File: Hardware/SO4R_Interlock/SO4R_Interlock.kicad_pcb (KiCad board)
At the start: 4 copper layers, 67.4 x 100.7 mm, 143 parts, among them J1 USB-C 2.0 16P, J2 USB-C 2.0 16P, J3 USB-C 2.0 16P, J4 USB-C 2.0 16P, J5 Header 1x3, J6 RJ45_LED_Shielded, J7 8P8C_LED_Shielded_x4, Q1 2N7002, Q2 2N7002, Q3 2N7002, Q4 2N7002, Q5 2N7002, Q6 2N7002, Q7 2N7002, Q8 2N7002, U1 FT230XS, U10 TPD4E02B04DQA, U11 TPD4E02B04DQA, U12 TPD4E02B04DQA, U2 FT230XS, U3 FT230XS, U4 FT230XS, U5 74LVC1G07, U6 74LVC1G07, U7 74LVC1G07, U8 AVR32DB48x-xPT, U9 TPD4E02B04DQA

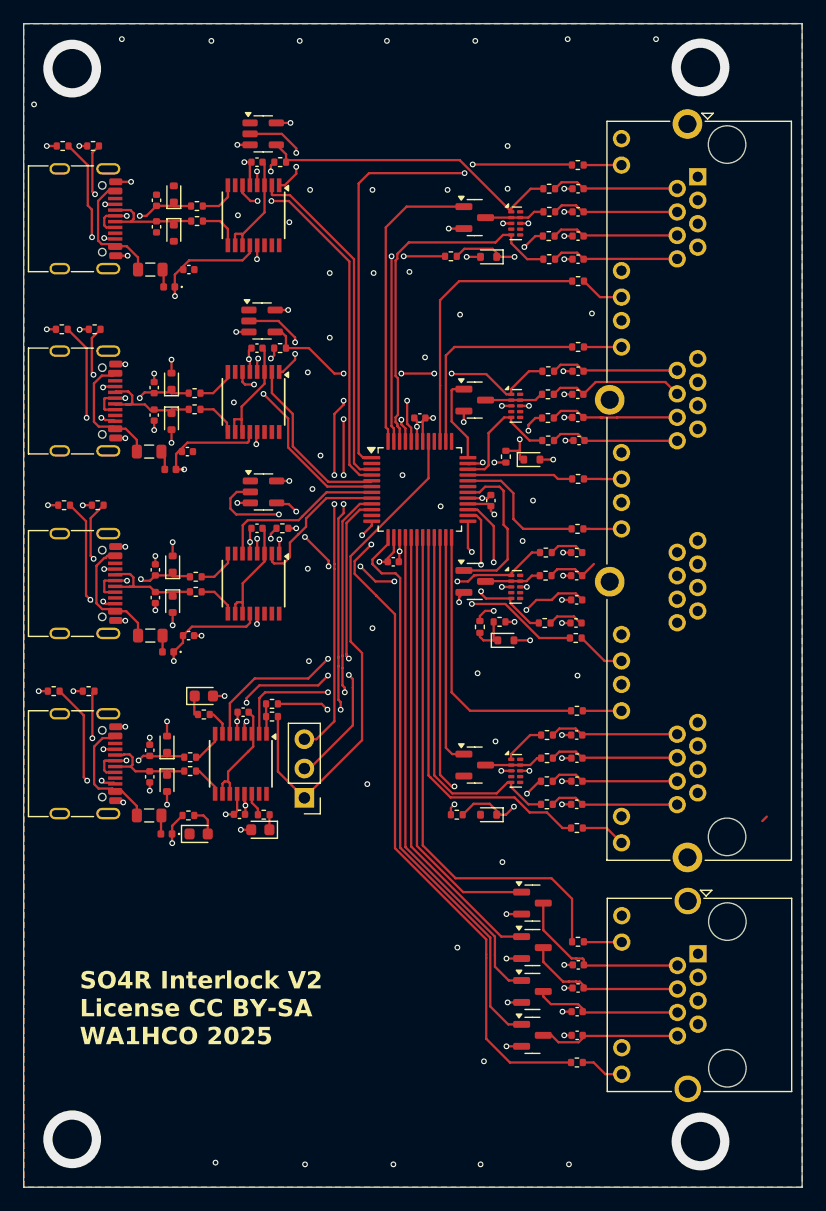
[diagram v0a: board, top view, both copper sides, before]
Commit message: V2 Files sent to JLCPCB Relays are driven by 12V Relay driver has diagnostic interface to MCU Diode combine 12V from rig interface or barrel jack
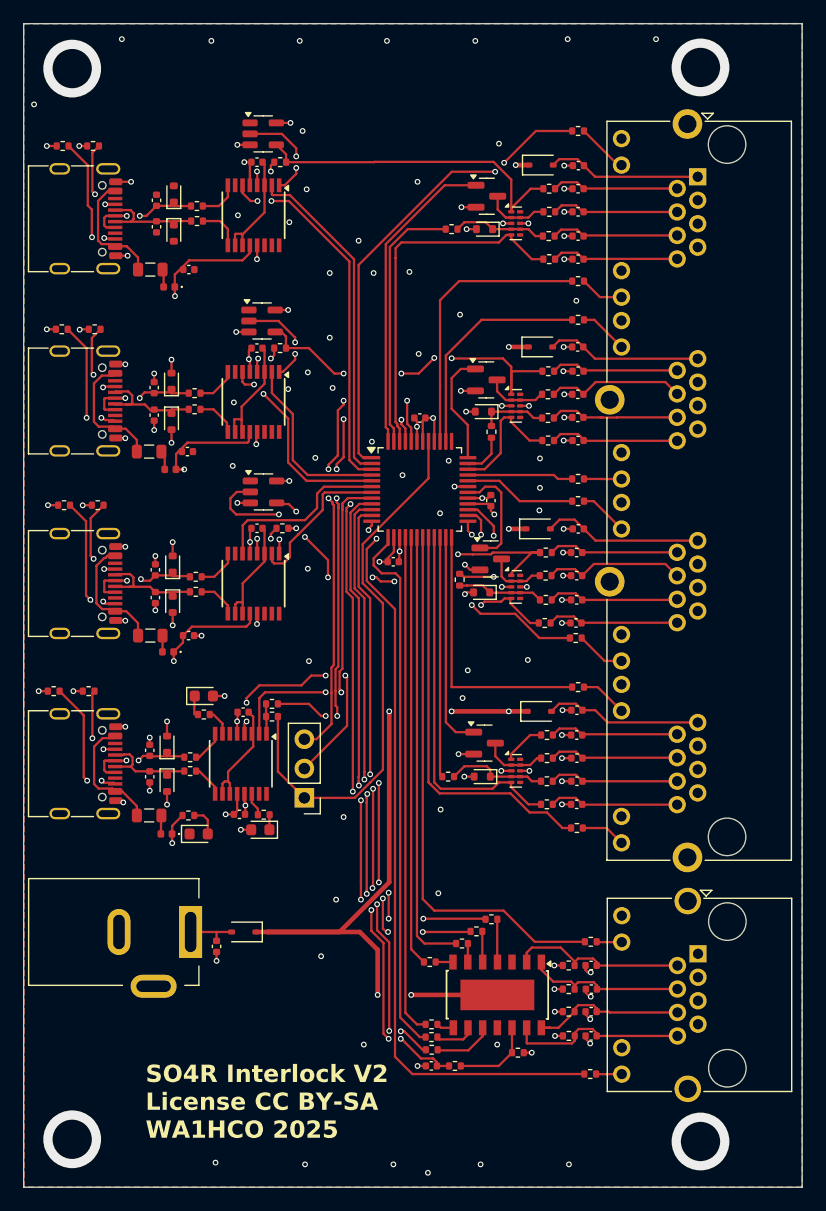
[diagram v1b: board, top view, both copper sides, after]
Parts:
- removed the C19 at (151.2, 131.5)
- removed the C21 at (151.1, 133.6)
- removed the C22 at (151.1, 135.6)
- removed the Q1 at (147.2, 124.2)
- removed the Q2 at (147.2, 128.0)
- removed the Q3 at (147.2, 131.8)
- removed the Q4 at (147.2, 135.6)
- added C1: .1u, Capacitor_SMD:C_0402_1005Metric, F.Cu at (119.9, 127.9)
- added C30: .1u, Capacitor_SMD:C_0402_1005Metric, F.Cu at (151.2, 60.3)
- added C32: .1u, Capacitor_SMD:C_0402_1005Metric, F.Cu at (151.2, 76.0)
- added C34: .1u, Capacitor_SMD:C_0402_1005Metric, F.Cu at (151.2, 91.8)
- added C36: .1u, Capacitor_SMD:C_0402_1005Metric, F.Cu at (151.1, 107.5)
- added C42: .1u, Capacitor_SMD:C_0402_1005Metric, F.Cu at (152.3, 135.7)
- added C43: .1u, Capacitor_SMD:C_0402_1005Metric, F.Cu at (152.3, 133.6)
- added C44: .1u, Capacitor_SMD:C_0402_1005Metric, F.Cu at (152.3, 129.6)
- added C45: .1u, Capacitor_SMD:C_0402_1005Metric, F.Cu at (152.3, 131.6)
- added D21: BAS316, Diode_SMD:D_SOD-323, F.Cu at (148.0, 60.2)
- added D22: BAS316, Diode_SMD:D_SOD-323, F.Cu at (147.8, 107.5)
- added D23: BAS316, Diode_SMD:D_SOD-323, F.Cu at (147.9, 76.0)
- added D24: BAS316, Diode_SMD:D_SOD-323, F.Cu at (147.8, 91.8)
- added D5: BAS316, Diode_SMD:D_SOD-323, F.Cu at (122.2, 126.7)
- added J1: 12V, Connector_BarrelJack:BarrelJack_Kycon_KLDX-0202-xC_Horizontal, F.Cu at (117.7, 126.7)
- added R25: 4K7, Resistor_SMD:R_0402_1005Metric, F.Cu at (140.5, 138.2)
- added R26: 10K, Resistor_SMD:R_0402_1005Metric, F.Cu at (138.5, 136.8)
- added R27: 10K, Resistor_SMD:R_0402_1005Metric, F.Cu at (138.4, 129.2)
- added R28: 10K, Resistor_SMD:R_0402_1005Metric, F.Cu at (141.2, 127.7)
- added R29: 10K, Resistor_SMD:R_0402_1005Metric, F.Cu at (138.5, 134.7)
- added R30: 10K, Resistor_SMD:R_0402_1005Metric, F.Cu at (138.5, 135.8)
- added R31: 10K, Resistor_SMD:R_0402_1005Metric, F.Cu at (142.4, 126.6)
- added R32: 10K, Resistor_SMD:R_0402_1005Metric, F.Cu at (143.7, 125.5)
- added R33: 1K2, Resistor_SMD:R_0402_1005Metric, F.Cu at (146.0, 137.1)
- added R34: 47k, Resistor_SMD:R_0402_1005Metric, F.Cu at (150.4, 135.7)
- added R35: 47K, Resistor_SMD:R_0402_1005Metric, F.Cu at (150.4, 133.6)
- added R36: 47K, Resistor_SMD:R_0402_1005Metric, F.Cu at (150.4, 129.6)
- added R37: 47K, Resistor_SMD:R_0402_1005Metric, F.Cu at (150.4, 131.6)
- added U8: BTS5200-4EKA, Interlock:Infineon_PG-DSO-14-48-EP, F.Cu at (144.2, 132.1)
- C18: value .1u -> 100p
- moved C18 15.4 mm to (138.5, 138.2), turned to 180 degrees
- moved D18 5.90 mm to (143.0, 81.6), turned to 180 degrees
- moved D19 4.65 mm to (142.8, 97.2), turned to 180 degrees
- moved R42 4.45 mm to (140.9, 96.2)
- moved R54 4.44 mm to (148.4, 97.9)
- moved R43 3.38 mm to (139.9, 113.2)
- moved D20 3.35 mm to (142.9, 113.2)
- moved R61 2.95 mm to (151.2, 57.3)
- moved R41 2.49 mm to (143.7, 83.3)
- moved D17 2.43 mm to (143.1, 65.8)
- moved R65 2.40 mm to (151.2, 89.3)
- moved Q3 2.39 mm to (143.6, 94.3)
- moved R40 2.35 mm to (140.2, 65.8)
- moved R63 2.35 mm to (151.2, 73.7)
- moved Q1 2.13 mm to (143.3, 63.0)
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- renumbered C9 to C10, C10 to C11, C11 to C12, C12 to C13, C13 to C14, C14 to C15, C15 to C16, C16 to C17, C17 to C19, C1 to C2, C23 to C21, C24 to C22, C25 to C23, C26 to C24, C27 to C25, C28 to C26, C29 to C27, C30 to C28, C31 to C29, C2 to C3, C32 to C31, C34 to C35, C35 to C37, C36 to C38, C37 to C39, C3 to C4, C38 to C40, C39 to C41, C4 to C5, C5 to C6, C6 to C7, C7 to C8, C8 to C9, D9 to D10, D10 to D11, D11 to D12, D12 to D13, D13 to D14, D14 to D15, D15 to D16, D19 to D17, D16 to D19, D17 to D20, D5 to D6, D6 to D7, D7 to D8, D8 to D9, J1 to J2, J2 to J3, J3 to J4, J4 to J5, J5 to J6, J6 to J7, J7 to J8, Q6 to Q1, Q7 to Q2, Q8 to Q3, Q5 to Q4, R26 to R38, R25 to R39, R57 to R40, R55 to R41, R52 to R42, R53 to R43, R27 to R44, R28 to R45, R58 to R46, R30 to R47, R31 to R48, R32 to R49, R56 to R50, R34 to R51, R35 to R52, R36 to R53, R51 to R54, R38 to R55, R39 to R56, R40 to R57, R54 to R58, R42 to R59, R43 to R60, R44 to R61, R45 to R62, R46 to R63, R47 to R64, R48 to R65, R49 to R66, R50 to R67, U9 to U10, U10 to U11, U11 to U12, U12 to U13, U8 to U9
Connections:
- C18 pad 1: GND -> /IS
- C18 pad 2: Net-(Q1-D) -> GND
- J7 pad 2: Net-(Q1-D) -> Net-(U8-OUT1)
- J8 pad 1: GND -> Net-(D21-A)
- J8 pad 13: GND -> Net-(D23-A)
- J8 pad 25: GND -> Net-(D24-A)
- J8 pad 37: GND -> Net-(D22-A)
- U10 pad 4: unconnected-(U9-IO3-Pad4) -> /KEY4\
- U11 pad 4: unconnected-(U10-IO3-Pad4) -> /KEY3\
- U12 pad 4: unconnected-(U11-IO3-Pad4) -> /KEY2\
- U13 pad 4: unconnected-(U12-IO3-Pad4) -> /KEY1\
- U4 pad 6: /CTS1\ -> unconnected-(U4-~{CTS}-Pad6)
- U9 pad 10: /CTS1\ -> /DSEL0
- U9 pad 11: unconnected-(U8-PC1-Pad11) -> /DSEL1
- U9 pad 2: unconnected-(U8-PA6-Pad2) -> /RTS4\
- U9 pad 3: /RTS4\ -> /CTS4\
- U9 pad 31: unconnected-(U8-PE1-Pad31) -> /IS
- U9 pad 4: /CTS4\ -> /RTS3\
- U9 pad 5: /RTS3\ -> /CTS3\
- U9 pad 6: /CTS3\ -> /CTS2\
- U9 pad 7: /CTS2\ -> /RTS2\
- U9 pad 8: /RTS2\ -> /RTS1\
- U9 pad 9: /RTS1\ -> /DEN
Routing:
- net /12V: track 0.00 -> 117.9 mm, vias 0 -> 8
- net /IS: track 0.00 -> 65.2 mm, vias 0 -> 8
- net /DEN: track 0.00 -> 52.5 mm, vias 0 -> 6
- net /DSEL0: track 0.00 -> 46.6 mm, vias 0 -> 6
- net /DSEL1: track 0.00 -> 45.5 mm, vias 0 -> 6
- net /CTS1\: track 29.6 -> 0.00 mm, vias 2 -> 0
- net Net-(U8-OUT1): track 0.00 -> 15.8 mm
- net Net-(Q1-D): track 15.5 -> 0.00 mm
- net Net-(D24-A): track 0.00 -> 13.8 mm
- net Net-(D22-A): track 0.00 -> 13.6 mm
- net Net-(D23-A): track 0.00 -> 13.5 mm
- net Net-(D21-A): track 0.00 -> 13.4 mm
- net Net-(C40-Pad2): track 3.18 -> 11.4 mm
- net Net-(C24-Pad2): track 3.14 -> 11.3 mm
- net Net-(C28-Pad2): track 4.62 -> 12.3 mm
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
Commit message: 2nd try at submitting to JLCPBC, this is hardware V2.1 V2 added BTS5200 relay driver chip, 4 channels Corrected footprints Adjusted HardwareConfig.h to adapt to new pins related to adding relay driver chip Software now has the ability detect faults on relay lines
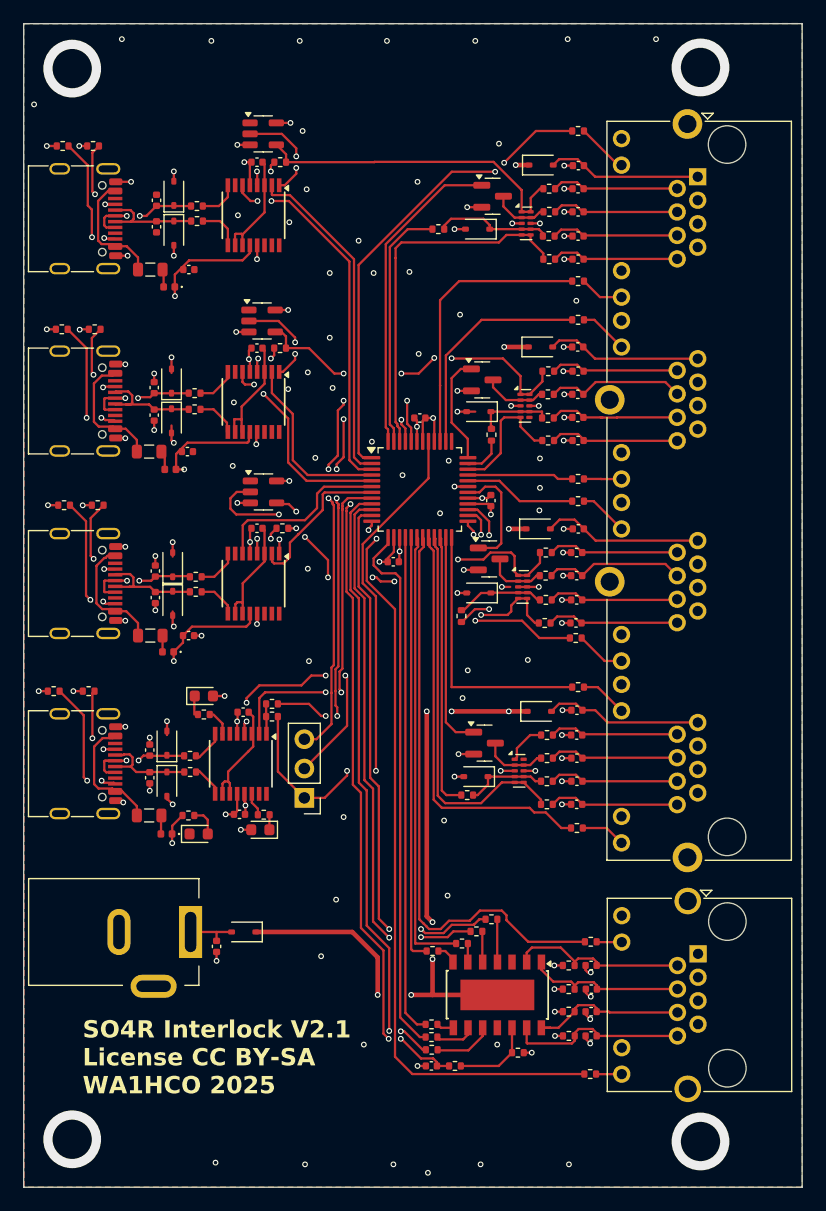
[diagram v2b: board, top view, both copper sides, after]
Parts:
- D1, D10, D11, D12, D13, D17, D18, D19, D2, D20, D3, D4: footprint Diode_SMD:D_SOD-523 -> Diode_SMD:D_SOD-323
- moved R42 3.15 mm to (141.1, 99.3), turned to -90 degrees
- moved R43 2.30 mm to (141.6, 114.8)
- moved R40 1.15 mm to (139.1, 65.8)
- moved R27 0.98 mm to (138.6, 128.3)
- moved U10 0.90 mm to (146.7, 65.3)
- moved U11 0.80 mm to (146.6, 81.1)
- moved D17 0.60 mm to (142.5, 65.8)
- moved U12 0.60 mm to (146.4, 96.8)
- moved D20 0.55 mm to (142.3, 113.2)
- moved Q1 0.50 mm to (143.8, 63.0)
- moved D18 0.40 mm to (142.6, 81.6)
- moved Q2 0.35 mm to (142.9, 78.8)
- moved U13 0.30 mm to (146.1, 112.7)
- moved D19 0.25 mm to (142.6, 97.3)
- moved R41 0.25 mm to (143.7, 83.6)
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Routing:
- net GND: track 84.6 -> 91.4 mm, vias 147 -> 149
- net /12V: track 117.9 -> 111.8 mm, vias 8 -> 10
- net /TX1: track 46.9 -> 50.0 mm
- net /KEY1\M: track 20.8 -> 23.8 mm
- net /KEY2\M: track 10.3 -> 12.7 mm
- net /SPR2: track 15.1 -> 17.1 mm
- net /KEY4\: track 8.19 -> 10.1 mm
- net /KEY1\: track 8.79 -> 7.12 mm
- net /SPR1: track 31.9 -> 33.5 mm
- net /DSEL1: track 45.5 -> 46.9 mm, vias 6 -> 2
- net /KEY4\M: track 22.5 -> 21.3 mm
- net /CAT3: track 30.5 -> 29.4 mm
- net /KEY3\: track 5.75 -> 6.62 mm
- net /RLY4: track 38.2 -> 38.8 mm
- net /UPDI: track 47.3 -> 46.7 mm, vias 0 -> 2
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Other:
- board text added: "SO4R Interlock V2.1 License CC BY-SA WA1HCO 2025"
- board text removed: "SO4R Interlock V2 License CC BY-SA WA1HCO 2025"

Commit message: Fix problem with 3.6V input protection zener leaking too much for input pullups, changed to 4V7 zener. initialize for loop index which was causing strange problems Fix labeling of RJ45 LED colors
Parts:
- D17, D18, D19, D20: value MM3Z3V6 -> MM3Z4V7
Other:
- board text added: "1"
- board text added: "12V"
- board text added: "2"
- board text added: "3"
- board text added: "4"
- board text added: "RLY"
- board text added: "SO4R Interlock V2.2 License CC BY-SA WA1HCO 2025"
- board text removed: "SO4R Interlock V2.1 License CC BY-SA WA1HCO 2025"
